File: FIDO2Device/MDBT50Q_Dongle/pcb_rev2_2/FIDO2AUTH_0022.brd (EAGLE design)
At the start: 19.5 x 34.3 mm, 40 parts, among them CN1 TE-1734028, CN2 IF_5PIN_H, SW1 SKRPACE010, SW2 SKTADAE010, U1 MDBT50Q-P1M, U2 XC6206P302MR-G, U4 RV-3028-C7, X1 NX3215SA-32.768K

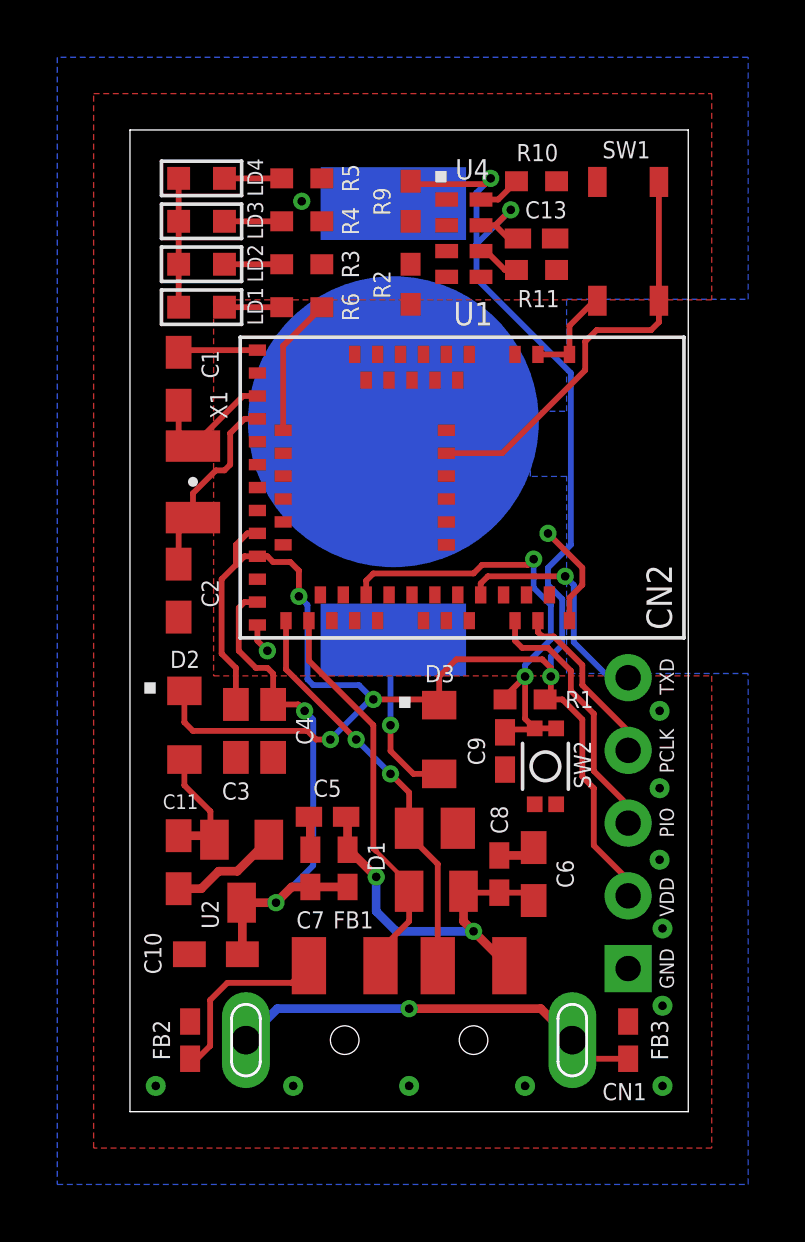
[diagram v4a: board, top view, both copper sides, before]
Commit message: 配線レイアウトを作成
・LED、TWI周りの配線を修正
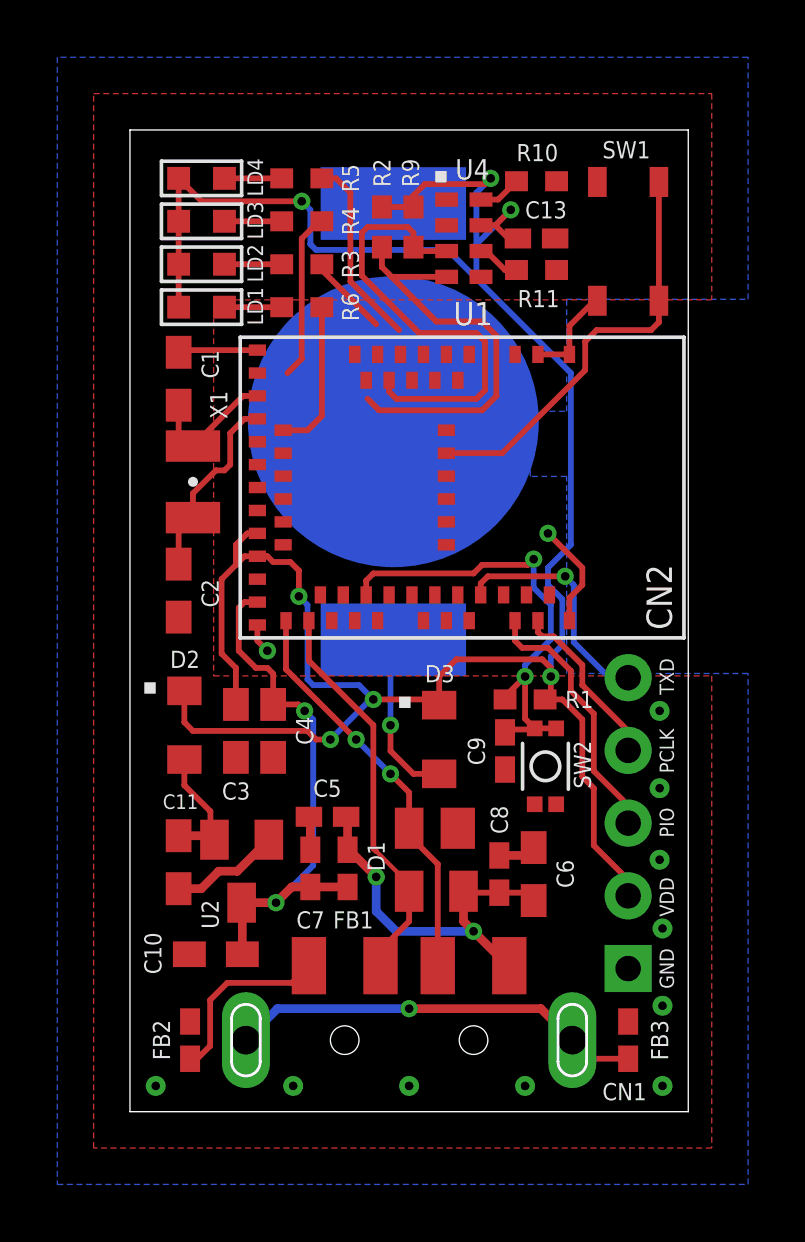
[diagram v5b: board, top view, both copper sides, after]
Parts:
- moved R2 2.24 mm to (8.80, 30.9), turned to 90 degrees
- moved R9 0.91 mm to (9.90, 30.9)
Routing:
- net TWI_SCL: track 0.00 -> 16.1 mm
- net TWI_SDA: track 0.00 -> 14.6 mm
- net VDD_NRF: track 72.8 -> 86.9 mm
- net LED4: track 0.00 -> 6.71 mm
- net LED3: track 0.00 -> 5.86 mm
- net LED2: track 0.00 -> 2.89 mm
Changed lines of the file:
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@@
 <layer number="100" name="Muster" color="7" fill="1" visible="no" active="no"/>
 <layer number="101" name="Patch_Top" color="12" fill="4" visible="no" active="yes"/>
-<layer number="102" name="Vscore" color="7" fill="1" visible="no" active="yes"/>
+<layer number="102" name="Vscore" color="7" fill="1" visible="yes" active="yes"/>
 <layer number="103" name="tMap" color="7" fill="1" visible="no" active="yes"/>
 <layer number="104" name="Name" color="7" fill="1" visible="no" active="yes"/>
@@
 <layer number="133" name="bottom_silk" color="7" fill="1" visible="no" active="no"/>
 <layer number="144" name="Drill_legend" color="7" fill="1" visible="no" active="yes"/>
-<layer number="150" name="Notes" color="7" fill="1" visible="no" active="yes"/>
+<layer number="150" name="Notes" color="7" fill="1" visible="yes" active="yes"/>
 <layer number="151" name="HeatSink" color="7" fill="1" visible="no" active="yes"/>
 <layer number="152" name="_bDocu" color="7" fill="1" visible="no" active="yes"/>
@@
 <attribute name="VALUE" x="9.56" y="32.16" size="0.7112" layer="27" rot="R270"/>
 </element>
-<element name="R2" library="Parts" package="R0402N" value="10k" x="9.8" y="28.9" smashed="yes" rot="R270">
-<attribute name="NAME" x="9.1" y="28.4" size="0.6" layer="25" rot="R90"/>
-<attribute name="VALUE" x="8.5" y="29.4" size="0.6" layer="27" rot="R270"/>
-</element>
-<element name="R9" library="Parts" package="R0402N" value="10k" x="9.8" y="31.8" smashed="yes" rot="R90">
-<attribute name="NAME" x="9.1" y="31.3" size="0.6" layer="25" rot="R90"/>
-<attribute name="VALUE" x="11.1" y="31.3" size="0.6" layer="27" rot="R90"/>
+<element name="R2" library="Parts" package="R0402N" value="10k" x="8.8" y="30.9" smashed="yes" rot="R90">
+<attribute name="NAME" x="9.1" y="32.3" size="0.6" layer="25" rot="R90"/>
+<attribute name="VALUE" x="10.1" y="30.4" size="0.6" layer="27" rot="R90"/>
+</element>
+<element name="R9" library="Parts" package="R0402N" value="10k" x="9.9" y="30.9" smashed="yes" rot="R90">
+<attribute name="NAME" x="10.1" y="32.3" size="0.6" layer="25" rot="R90"/>
+<attribute name="VALUE" x="11.2" y="30.4" size="0.6" layer="27" rot="R90"/>
 </element>
 <element name="R10" library="Parts" package="R0402N" value="10k" x="14.2" y="32.5" smashed="yes" rot="R180">
@@
 <wire x1="12.6" y1="32.6" x2="12.1" y2="32.1" width="0.2032" layer="16"/>
 <wire x1="12.1" y1="32.1" x2="12.1" y2="30.3" width="0.2032" layer="16"/>
-<wire x1="9.8" y1="32.5" x2="9.9" y2="32.4" width="0.2032" layer="1"/>
-<wire x1="9.9" y1="32.4" x2="12.4" y2="32.4" width="0.2032" layer="1"/>
-<wire x1="12.4" y1="32.4" x2="12.6" y2="32.6" width="0.2032" layer="1"/>
 <wire x1="15.1" y1="14.4" x2="14.5" y2="14.4" width="0.2032" layer="1"/>
 <wire x1="14.4" y1="15.8" x2="11.4" y2="15.8" width="0.2032" layer="1"/>
@@
 <wire x1="3.7" y1="15.5" x2="3.2" y2="16" width="0.2032" layer="1"/>
 <wire x1="1.7" y1="32.6" x2="1.7" y2="31.1" width="0.2032" layer="1"/>
-<wire x1="12.1" y1="29.1" x2="9.8" y2="28.2" width="0" layer="19" extent="1-16"/>
-<wire x1="6" y1="31.8" x2="9.8" y2="32.5" width="0" layer="19" extent="1-1"/>
-<wire x1="1.7" y1="32.6" x2="6" y2="31.8" width="0" layer="19" extent="1-1"/>
+<wire x1="6" y1="31.8" x2="6.3" y2="31.5" width="0.2032" layer="16"/>
+<wire x1="6.3" y1="31.5" x2="6.3" y2="30.3" width="0.2032" layer="16"/>
+<wire x1="6.3" y1="30.3" x2="6.5" y2="30.1" width="0.2032" layer="16"/>
+<wire x1="6.5" y1="30.1" x2="11.1" y2="30.1" width="0.2032" layer="16"/>
+<wire x1="11.1" y1="30.1" x2="12.1" y2="29.1" width="0.2032" layer="16"/>
+<wire x1="6" y1="31.8" x2="2.5" y2="31.8" width="0.2032" layer="1"/>
+<wire x1="2.5" y1="31.8" x2="1.7" y2="32.6" width="0.2032" layer="1"/>
+<wire x1="8.8" y1="31.6" x2="9.9" y2="31.6" width="0.2032" layer="1"/>
+<wire x1="9.9" y1="31.6" x2="9.9" y2="32" width="0.2032" layer="1"/>
+<wire x1="9.9" y1="32" x2="10.3" y2="32.4" width="0.2032" layer="1"/>
+<wire x1="10.3" y1="32.4" x2="12.4" y2="32.4" width="0.2032" layer="1"/>
+<wire x1="12.4" y1="32.4" x2="12.6" y2="32.6" width="0.2032" layer="1"/>
 </signal>
 <signal name="VBUS">
@@
 <contactref element="U1" pad="24"/>
 <contactref element="R3" pad="1"/>
-<wire x1="4.45" y1="21.8" x2="6.7" y2="29.6" width="0" layer="19" extent="1-1"/>
+<wire x1="6.7" y1="29.6" x2="6.7" y2="29.4" width="0.2032" layer="1"/>
+<wire x1="6.7" y1="29.4" x2="8.6" y2="27.5" width="0.2032" layer="1"/>
+<wire x1="4.45" y1="21.8" x2="8.6" y2="27.5" width="0" layer="19" extent="1-1"/>
 </signal>
 <signal name="LED3">
 <contactref element="U1" pad="26"/>
 <contactref element="R4" pad="1"/>
-<wire x1="4.45" y1="21" x2="6.7" y2="31.1" width="0" layer="19" extent="1-1"/>
+<wire x1="6.7" y1="31.1" x2="6.6" y2="31.1" width="0.2032" layer="1"/>
+<wire x1="6.6" y1="31.1" x2="6" y2="30.5" width="0.2032" layer="1"/>
+<wire x1="6" y1="30.5" x2="6" y2="26.3" width="0.2032" layer="1"/>
+<wire x1="6" y1="26.3" x2="5.5" y2="25.8" width="0.2032" layer="1"/>
+<wire x1="4.45" y1="21" x2="5.5" y2="25.8" width="0" layer="19" extent="1-1"/>
 </signal>
 <signal name="LED4">
 <contactref element="U1" pad="29"/>
 <contactref element="R5" pad="1"/>
-<wire x1="5.35" y1="19.8" x2="6.7" y2="32.6" width="0" layer="19" extent="1-1"/>
+<wire x1="6.7" y1="32.6" x2="7.2" y2="32.6" width="0.2032" layer="1"/>
+<wire x1="7.2" y1="32.6" x2="7.7" y2="32.1" width="0.2032" layer="1"/>
+<wire x1="7.7" y1="32.1" x2="7.7" y2="29" width="0.2032" layer="1"/>
+<wire x1="7.7" y1="29" x2="9.4" y2="27.3" width="0.2032" layer="1"/>
+<wire x1="5.35" y1="19.8" x2="9.4" y2="27.3" width="0" layer="19" extent="1-1"/>
 </signal>
 <signal name="SW1">
@@
 <contactref element="U4" pad="3"/>
 <contactref element="R9" pad="1"/>
-<wire x1="9.8" y1="31.1" x2="11.06" y2="30.06" width="0" layer="19" extent="1-1"/>
-<wire x1="9.05" y1="25.55" x2="11.06" y2="30.06" width="0" layer="19" extent="1-1"/>
+<wire x1="9.9" y1="30.2" x2="9.9" y2="30.7" width="0.2032" layer="1"/>
+<wire x1="9.9" y1="30.7" x2="9.7" y2="30.9" width="0.2032" layer="1"/>
+<wire x1="9.7" y1="30.9" x2="8.3" y2="30.9" width="0.2032" layer="1"/>
+<wire x1="8.3" y1="30.9" x2="8.1" y2="30.7" width="0.2032" layer="1"/>
+<wire x1="8.1" y1="30.7" x2="8.1" y2="29.2" width="0.2032" layer="1"/>
+<wire x1="8.1" y1="29.2" x2="10.1" y2="27.2" width="0.2032" layer="1"/>
+<wire x1="10.1" y1="27.2" x2="12.1" y2="27.2" width="0.2032" layer="1"/>
+<wire x1="12.1" y1="27.2" x2="12.4" y2="26.9" width="0.2032" layer="1"/>
+<wire x1="12.4" y1="26.9" x2="12.4" y2="25.2" width="0.2032" layer="1"/>
+<wire x1="12.4" y1="25.2" x2="12.1" y2="24.9" width="0.2032" layer="1"/>
+<wire x1="12.1" y1="24.9" x2="9.3" y2="24.9" width="0.2032" layer="1"/>
+<wire x1="9.05" y1="25.55" x2="9.05" y2="25.15" width="0.2032" layer="1"/>
+<wire x1="9.05" y1="25.15" x2="9.3" y2="24.9" width="0.2032" layer="1"/>
+<wire x1="11.06" y1="30.06" x2="10.04" y2="30.06" width="0.2032" layer="1"/>
+<wire x1="10.04" y1="30.06" x2="9.9" y2="30.2" width="0.2032" layer="1"/>
 </signal>
 <signal name="N$8">
@@
 <contactref element="U4" pad="4"/>
 <contactref element="R2" pad="1"/>
-<wire x1="9.8" y1="29.6" x2="11.06" y2="29.16" width="0" layer="19" extent="1-1"/>
-<wire x1="4.45" y1="22.6" x2="9.8" y2="29.6" width="0" layer="19" extent="1-1"/>
+<wire x1="11.06" y1="29.16" x2="9.14" y2="29.16" width="0.2032" layer="1"/>
+<wire x1="9.14" y1="29.16" x2="8.8" y2="29.5" width="0.2032" layer="1"/>
+<wire x1="8.8" y1="29.5" x2="8.8" y2="30.2" width="0.2032" layer="1"/>
+<wire x1="9.14" y1="29.16" x2="10.7" y2="27.6" width="0.2032" layer="1"/>
+<wire x1="10.7" y1="27.6" x2="12.3" y2="27.6" width="0.2032" layer="1"/>
+<wire x1="12.3" y1="27.6" x2="12.8" y2="27.1" width="0.2032" layer="1"/>
+<wire x1="12.8" y1="27.1" x2="12.8" y2="25" width="0.2032" layer="1"/>
+<wire x1="12.8" y1="25" x2="12.3" y2="24.5" width="0.2032" layer="1"/>
+<wire x1="12.3" y1="24.5" x2="8.7" y2="24.5" width="0.2032" layer="1"/>
+<wire x1="8.7" y1="24.5" x2="8.3" y2="24.9" width="0.2032" layer="1"/>
+<wire x1="4.45" y1="22.6" x2="8.3" y2="24.9" width="0" layer="19" extent="1-1"/>
 </signal>
 <signal name="LED1">
 <contactref element="U1" pad="19"/>
 <contactref element="R6" pad="1"/>
-<wire x1="5.35" y1="23.8" x2="5.35" y2="26.75" width="0.2032" layer="1"/>
-<wire x1="5.35" y1="26.75" x2="6.7" y2="28.1" width="0.2032" layer="1"/>
+<wire x1="6.7" y1="28.1" x2="6.7" y2="24.3" width="0.2032" layer="1"/>
+<wire x1="6.7" y1="24.3" x2="6.2" y2="23.8" width="0.2032" layer="1"/>
+<wire x1="6.2" y1="23.8" x2="5.35" y2="23.8" width="0.2032" layer="1"/>
 </signal>
 <signal name="TXD">

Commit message: 配線レイアウトを作成
・LED2、LED3を残し、配線を完了
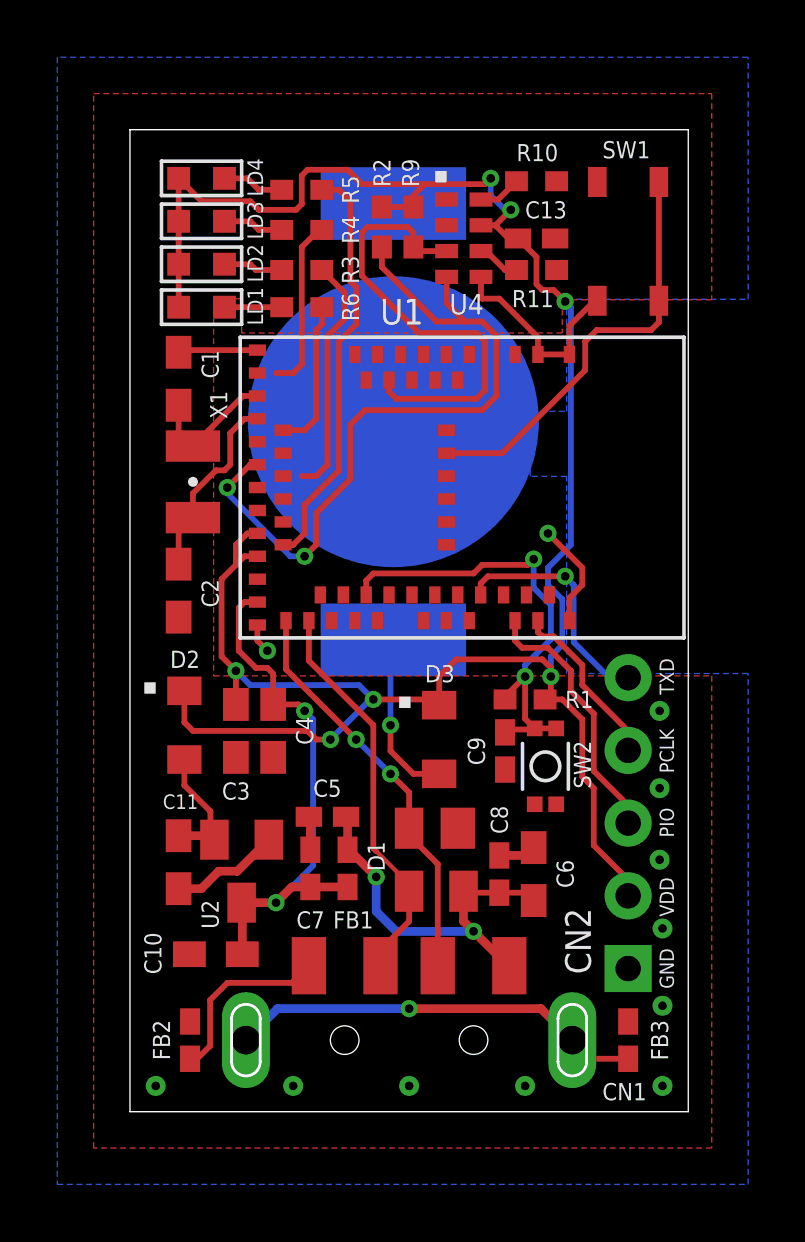
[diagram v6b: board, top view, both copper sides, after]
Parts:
- moved R5 0.40 mm to (6.00, 32.2)
- moved R4 0.30 mm to (6.00, 30.8)
- moved R3 0.20 mm to (6.00, 29.4)
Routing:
- net TWI_SDA: track 14.6 -> 25.6 mm, vias 0 -> 2
- net VDD_NRF: track 86.9 -> 78.9 mm
- net LED4: track 6.71 -> 14.5 mm
- net LED2: track 2.89 -> 8.45 mm
- net 0V: track 17.3 -> 21.2 mm

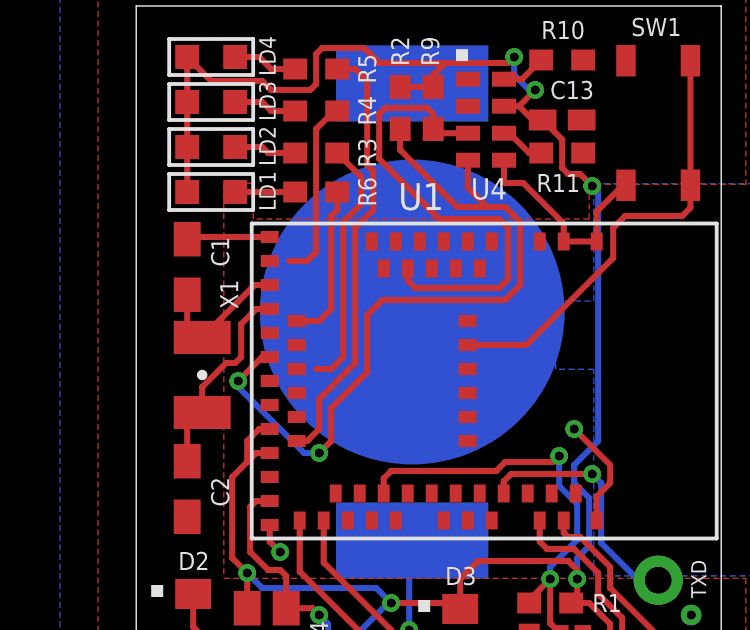
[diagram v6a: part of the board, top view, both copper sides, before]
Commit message: 配線レイアウトを修正
・LED2、LED3の配線を確定
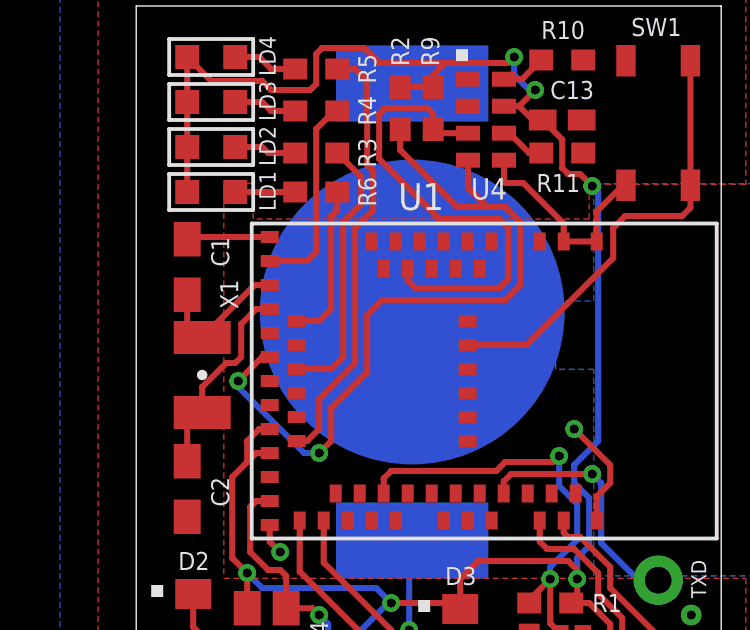
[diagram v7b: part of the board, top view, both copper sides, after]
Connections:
- net LED2: now also U1.23; no longer U1.24
- net LED3: now also U1.16; no longer U1.26
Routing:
- net LED3: track 6.07 -> 6.72 mm
- net LED2: track 8.45 -> 9.10 mm
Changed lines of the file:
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@@
 </signal>
 <signal name="LED2">
-<contactref element="U1" pad="24"/>
 <contactref element="R3" pad="1"/>
 <wire x1="6.7" y1="29.4" x2="7.5" y2="28.6" width="0.2032" layer="1"/>
@@
 <wire x1="6.9" y1="27.1" x2="6.9" y2="22.6" width="0.2032" layer="1"/>
 <wire x1="6.9" y1="22.6" x2="6.5" y2="22.2" width="0.2032" layer="1"/>
-<wire x1="6.5" y1="22.2" x2="6" y2="22.2" width="0.2032" layer="1"/>
-<wire x1="4.45" y1="21.8" x2="6" y2="22.2" width="0" layer="19" extent="1-1"/>
+<contactref element="U1" pad="23"/>
+<wire x1="5.35" y1="22.2" x2="6.5" y2="22.2" width="0.2032" layer="1"/>
 </signal>
 <signal name="LED3">
-<contactref element="U1" pad="26"/>
 <contactref element="R4" pad="1"/>
 <wire x1="6.7" y1="30.8" x2="6.6" y2="30.8" width="0.2032" layer="1"/>
@@
 <wire x1="6" y1="30.2" x2="6" y2="26.1" width="0.2032" layer="1"/>
 <wire x1="6" y1="26.1" x2="5.7" y2="25.8" width="0.2032" layer="1"/>
-<wire x1="5.7" y1="25.8" x2="5.1" y2="25.8" width="0.2032" layer="1"/>
-<wire x1="4.45" y1="21" x2="5.1" y2="25.8" width="0" layer="19" extent="1-1"/>
+<contactref element="U1" pad="16"/>
+<wire x1="4.45" y1="25.8" x2="5.7" y2="25.8" width="0.2032" layer="1"/>
 </signal>
 <signal name="LED4">
